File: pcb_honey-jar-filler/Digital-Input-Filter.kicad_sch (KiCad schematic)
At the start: 3 parts

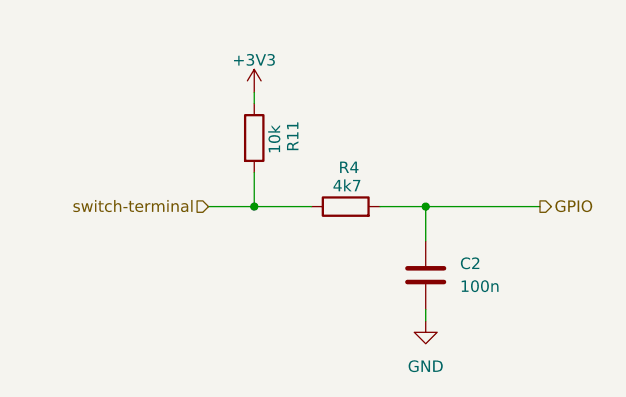
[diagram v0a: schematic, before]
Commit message: pcb: arrange parts, re-assign, add servo-cutoff
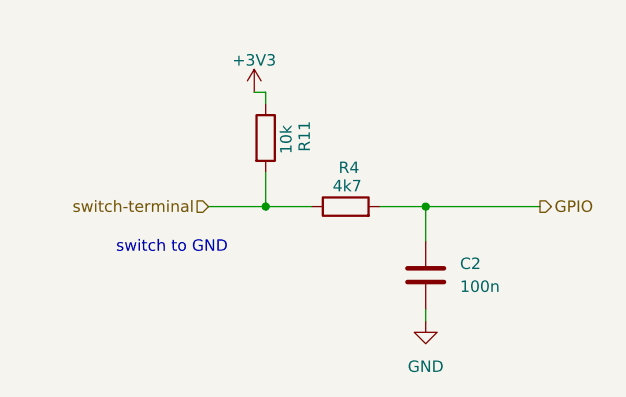
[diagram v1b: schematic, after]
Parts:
- R11, R4: footprint Resistor_THT:R_Axial_DIN0207_L6.3mm_D2.5mm_P2.54mm_Vertical -> Resistor_THT:R_Axial_DIN0207_L6.3mm_D2.5mm_P10.16mm_Horizontal
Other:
- note added: "switch to GND"
- moved on the sheet: R11
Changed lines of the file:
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@@
 	(generator_version "9.0")
 	(paper "A4")
+	(text "switch to GND"
+		(exclude_from_sim no)
+		(at 54.356 41.402 0)
+		(effects
+			(font
+				(size 1.27 1.27)
+			)
+		)
+	)
 	(junction
-		(at 63.5 36.83)
+		(at 64.77 36.83)
 		(diameter 0)
 		(color 0 0 0 0)
@@
 	(wire
 		(pts
-			(xy 58.42 36.83) (xy 63.5 36.83)
+			(xy 58.42 36.83) (xy 64.77 36.83)
+		)
+		(stroke
+			(width 0)
+			(type default)
+		)
+	)
+	(wire
+		(pts
+			(xy 64.77 36.83) (xy 69.85 36.83)
 		)
 		(stroke
@@
 	(wire
 		(pts
-			(xy 63.5 33.02) (xy 63.5 36.83)
-		)
-		(stroke
-			(width 0)
-			(type default)
-		)
-	)
-	(wire
-		(pts
-			(xy 63.5 36.83) (xy 69.85 36.83)
+			(xy 64.77 33.02) (xy 64.77 36.83)
 		)
 		(stroke
@@
 	(wire
 		(pts
+			(xy 64.77 24.13) (xy 63.5 24.13)
+		)
+		(stroke
+			(width 0)
+			(type default)
+		)
+	)
+	(wire
+		(pts
 			(xy 82.55 36.83) (xy 95.25 36.83)
 		)
@@
 	(wire
 		(pts
-			(xy 63.5 24.13) (xy 63.5 25.4)
+			(xy 64.77 24.13) (xy 64.77 25.4)
 		)
 		(stroke
@@
 			)
 		)
-		(property "Footprint" "Resistor_THT:R_Axial_DIN0207_L6.3mm_D2.5mm_P2.54mm_Vertical"
+		(property "Footprint" "Resistor_THT:R_Axial_DIN0207_L6.3mm_D2.5mm_P10.16mm_Horizontal"
 			(at 73.66 38.608 90)
 			(effects
@@
 	(symbol
 		(lib_id "Device:R")
-		(at 63.5 29.21 0)
+		(at 64.77 29.21 0)
 		(unit 1)
 		(exclude_from_sim no)
@@
 		(dnp no)
 		(property "Reference" "R11"
-			(at 67.818 30.734 90)
+			(at 69.088 30.734 90)
 			(effects
 				(font
@@
 		)
 		(property "Value" "10k"
-			(at 65.786 30.988 90)
+			(at 67.056 30.988 90)
 			(effects
 				(font
@@
 			)
 		)
-		(property "Footprint" "Resistor_THT:R_Axial_DIN0207_L6.3mm_D2.5mm_P2.54mm_Vertical"
-			(at 61.722 29.21 90)
+		(property "Footprint" "Resistor_THT:R_Axial_DIN0207_L6.3mm_D2.5mm_P10.16mm_Horizontal"
+			(at 62.992 29.21 90)
 			(effects
 				(font
@@
 		)
 		(property "Datasheet" "~"
-			(at 63.5 29.21 0)
+			(at 64.77 29.21 0)
 			(effects
 				(font
@@
 		)
 		(property "Description" "Resistor"
-			(at 63.5 29.21 0)
-			(effects
-				(font
+			(at 64.77 29.21 0)
+			(effects
+				(font

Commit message: pcb: Update actually soldered filter R values (use sub-sheet parameters)
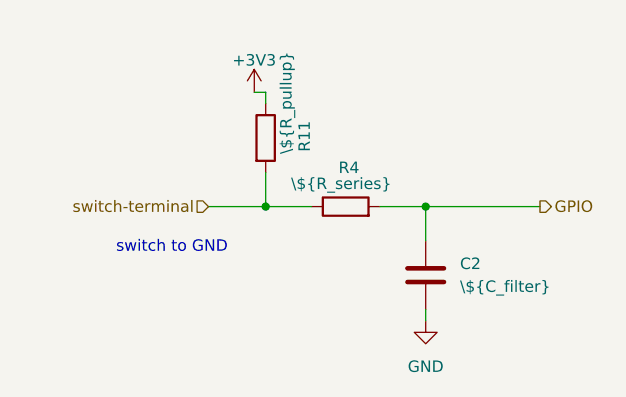
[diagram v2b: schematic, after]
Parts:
- C2: value 100n -> \${C_filter}
- R11: value 10k -> \${R_pullup}
- R4: value 4k7 -> \${R_series}
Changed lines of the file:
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@@
 			)
 		)
-		(property "Value" "100n"
+		(property "Value" "\\${C_filter}"
 			(at 86.36 45.7199 0)
 			(effects
@@
 			)
 		)
-		(property "Value" "4k7"
-			(at 75.438 34.544 90)
+		(property "Value" "\\${R_series}"
+			(at 78.74 34.29 90)
 			(effects
 				(font
@@
 			)
 		)
-		(property "Value" "10k"
+		(property "Value" "\\${R_pullup}"
 			(at 67.056 30.988 90)
 			(effects
